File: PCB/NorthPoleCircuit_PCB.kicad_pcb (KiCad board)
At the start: 4 copper layers, 150 x 110 mm, 105 parts, among them J1 USB_C_Receptacle_USB2.0_16P, J2 PROG, J3 PROG, U1 DRV8833PWP, U2 DRV8833PWP, U3 CH32V003FxUx, U4 CH32V003FxUx

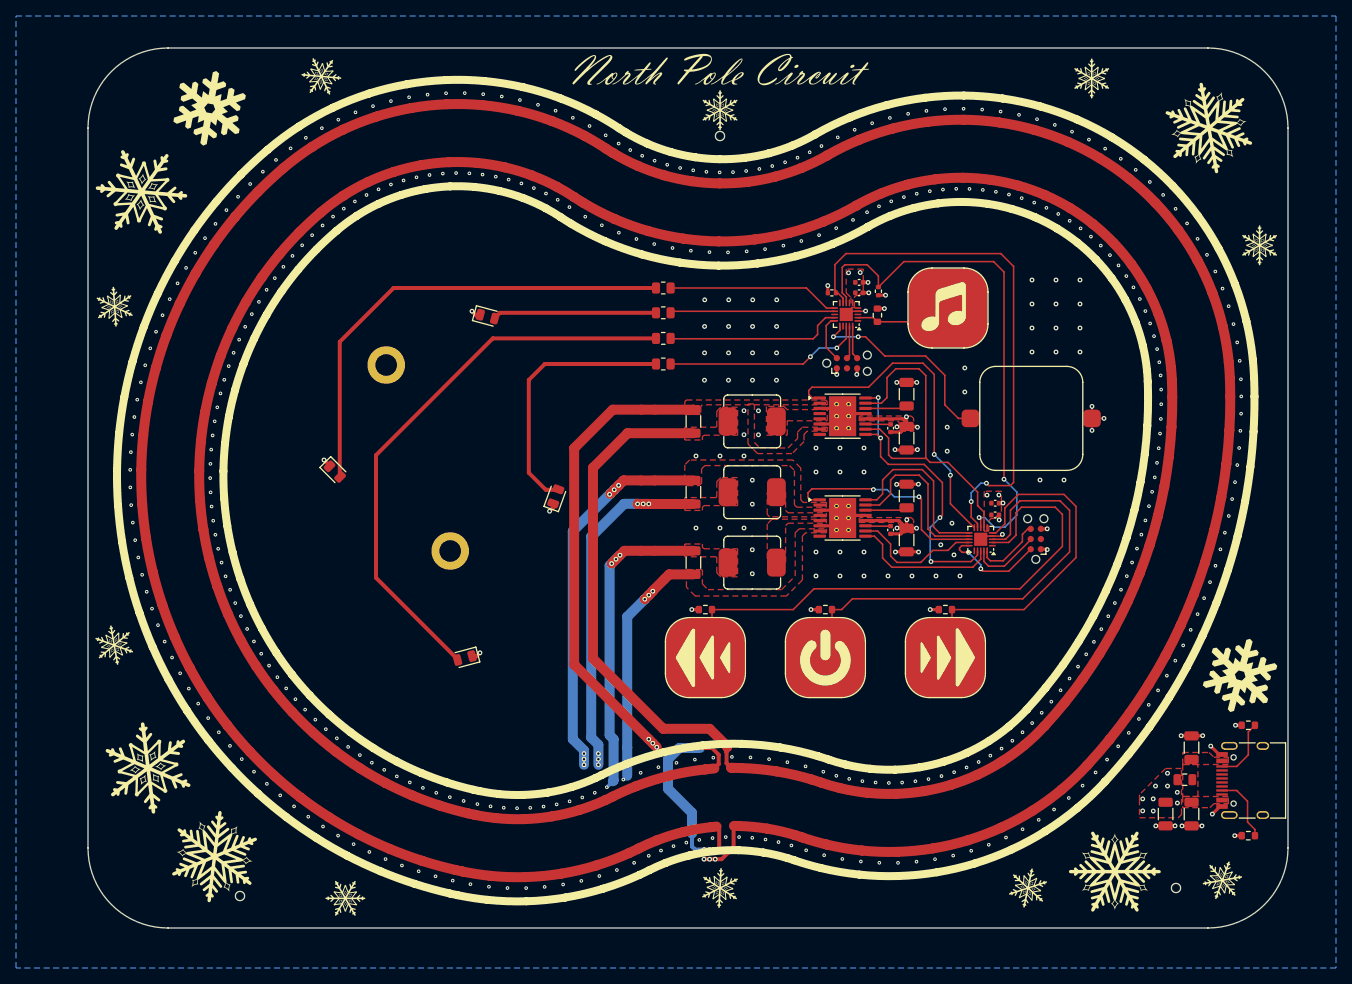
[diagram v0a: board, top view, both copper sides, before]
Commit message: Add BLE audio card hardware revision
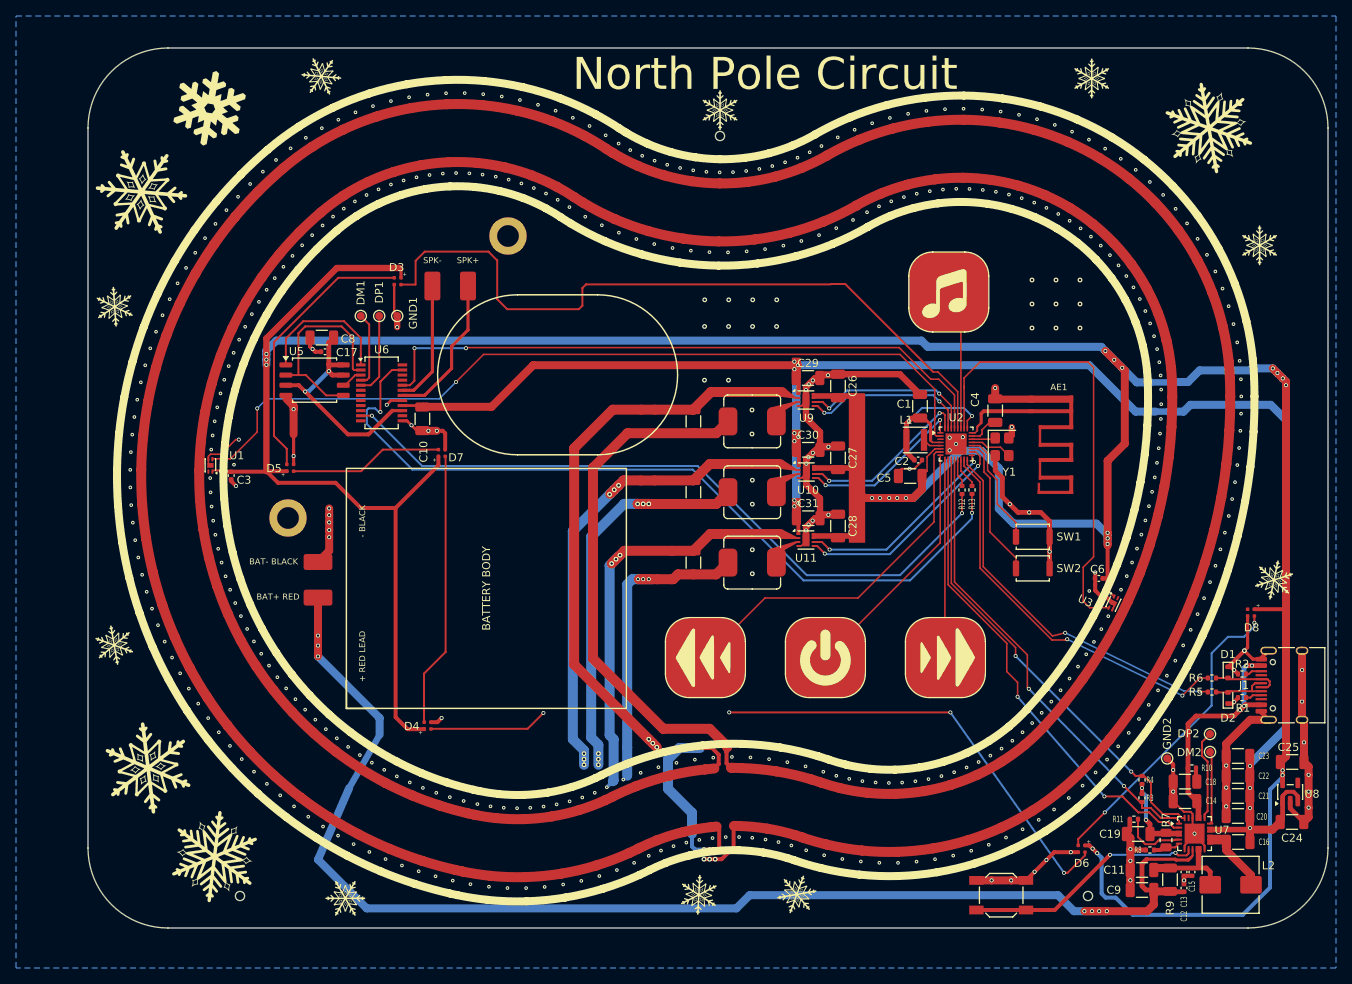
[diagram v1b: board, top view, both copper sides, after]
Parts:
- removed BZ1: FUET-1325H, cust_fp:FUET-1325
- removed the C10 at (165.3, 100.2)
- removed F1: 500mA, Fuse:Fuse_0805_2012Metric
- removed the G*** at (193.3, 142.9)
- removed the G*** at (148.8, 43.4)
- removed the G*** at (208.9, 118.4)
- removed the G*** at (140.8, 121.8)
- removed the G*** at (108.4, 130.2)
- removed the G*** at (108.9, 139.4)
- removed the G*** at (140.0, 67.8)
- removed the G*** at (152.5, 139.7)
- removed the G*** at (133.0, 83.5)
- removed the G*** at (157.6, 130.3)
- removed J2, J3: PROG, Connector:Tag-Connect_TC2030-IDC-NL_2x03_P1.27mm_Vertical
- removed the R3 at (136.9, 76.3)
- removed the R4 at (136.9, 73.1)
- removed U4: CH32V003FxUx, Package_DFN_QFN:QFN-20-1EP_3x3mm_P0.4mm_EP1.65x1.65mm
- added AE1: Bluetooth Antenna, cust_fp:WCH_ANT_F_1_2_4G_1p0mmFR4_12p3x5p6, F.Cu at (183.1, 85.4)
- added BAT_PAD1: BAT_PAD, cust_fp:Battery_LiPo_500mAh_30x35x4mm_WirePads, F.Cu at (93.8, 106.5)
- added BT1_BODY: LiPo_1S_500mAh, cust_fp:Battery_LiPo_500mAh_30x35x4mm_Body, F.Cu at (114.8, 107.5)
- added C11: 10uF, Capacitor_SMD:C_1206_3216Metric, F.Cu at (196.8, 142.8)
- added C12: 100nF, Capacitor_SMD:C_0402_1005Metric, F.Cu at (202.0, 145.0)
- added C16: 2.2uF, Capacitor_SMD:C_1206_3216Metric, F.Cu at (208.8, 139.2)
- added C17: 10uF, Capacitor_SMD:C_1206_3216Metric, F.Cu at (94.2, 76.2)
- added C18: 10uF, Capacitor_SMD:C_1206_3216Metric, F.Cu at (202.1, 131.7)
- added C19: 2.2uF, Capacitor_SMD:C_1206_3216Metric, F.Cu at (196.3, 138.2)
- added C20: 10uF, Capacitor_SMD:C_1206_3216Metric, F.Cu at (208.8, 136.0)
- added C21: 10uF, Capacitor_SMD:C_1206_3216Metric, F.Cu at (208.8, 133.5)
- added C22: 22uF, Capacitor_SMD:C_1206_3216Metric, F.Cu at (208.8, 131.0)
- added C23: 22uF, Capacitor_SMD:C_1206_3216Metric, F.Cu at (208.8, 128.5)
- added C24: 1uF, Capacitor_SMD:C_1206_3216Metric, F.Cu at (215.5, 136.8)
- added C25: 1uF, Capacitor_SMD:C_1206_3216Metric, F.Cu at (215.5, 129.2)
- added C28: 2.2uF, Capacitor_SMD:C_1206_3216Metric, F.Cu at (158.8, 99.8)
- added C31: 10uF, Capacitor_SMD:C_1206_3216Metric, F.Cu at (155.0, 98.8)
- added C4: 470nF, Capacitor_SMD:C_1206_3216Metric, F.Cu at (178.4, 85.3)
- added C5: 2.2uF, Capacitor_SMD:C_1206_3216Metric, F.Cu at (167.8, 93.5)
- added C8: 100nF, Capacitor_SMD:C_0402_1005Metric, F.Cu at (94.6, 78.0)
- added C9: 10uF, Capacitor_SMD:C_1206_3216Metric, F.Cu at (196.8, 145.2)
- added D5: TZ-H1010-RGB/A-BU08UF-TA1305NA/W109, cust_fp:ws2812b_1010, F.Cu at (90.3, 92.5)
- added D6: TZ-H1010-RGB/A-BU08UF-TA1305NA/W109, cust_fp:ws2812b_1010, F.Cu at (189.2, 140.1)
- added D7: TZ-H1010-RGB/A-BU08UF-TA1305NA/W109, cust_fp:ws2812b_1010, F.Cu at (109.2, 90.6)
- added D8: TZ-H1010-RGB/A-BU08UF-TA1305NA/W109, cust_fp:ws2812b_1010, F.Cu at (210.4, 110.6)
- added DM1: TestPoint_Small, TestPoint:TestPoint_Pad_D1.0mm, F.Cu at (99.1, 73.5)
- added DM2: TestPoint_Small, TestPoint:TestPoint_Pad_D1.0mm, F.Cu at (205.2, 128.0)
- added DP1: TestPoint_Small, TestPoint:TestPoint_Pad_D1.0mm, F.Cu at (101.4, 73.5)
- added DP2: TestPoint_Small, TestPoint:TestPoint_Pad_D1.0mm, F.Cu at (205.2, 125.8)
- added GND1: TestPoint_Small, TestPoint:TestPoint_Pad_D1.0mm, F.Cu at (103.7, 73.5)
- added GND2: TestPoint_Small, TestPoint:TestPoint_Pad_D1.0mm, F.Cu at (199.9, 128.8)
- added L1: ZENR3015T100M-10uH, Inductor_SMD:L_Taiyo-Yuden_NR-30xx, F.Cu at (168.4, 89.0)
- added L2: 1uH, Inductor_SMD:L_Wuerth_HCI-7030, F.Cu at (207.8, 144.6)
- added LS1_BODY: GSPK3020035PN-8R0.8W, cust_fp:Speaker_GSPK3020035PN_Body, F.Cu at (123.7, 80.8)
- added R11: 100kΩ, Resistor_SMD:R_0402_1005Metric, F.Cu at (195.7, 136.4)
- added R12: 2.7kΩ, Resistor_SMD:R_0402_1005Metric, F.Cu at (174.2, 95.2)
- added R13: 2.7kΩ, Resistor_SMD:R_0402_1005Metric, F.Cu at (175.5, 95.2)
- added SP_PAD1: SPK_PAD, cust_fp:Speaker_GSPK3020035PN_WirePads, F.Cu at (110.3, 69.8)
- added SW1: TS-1088-AR02016, Button_Switch_SMD:SW_Push_SPST_NO_Alps_SKRK, F.Cu at (183.1, 101.1)
- added SW2: TS-1088-AR02016, Button_Switch_SMD:SW_Push_SPST_NO_Alps_SKRK, F.Cu at (183.1, 105.0)
- added SW3: TS-1187A-C-E-B, Button_Switch_SMD:SW_SPST_SKQG_WithStem, F.Cu at (179.2, 145.9)
- added U10: DRV8837, Package_SON:WSON-8-1EP_2x2mm_P0.5mm_EP0.9x1.6mm, F.Cu at (154.8, 93.0)
- added U11: DRV8837, Package_SON:WSON-8-1EP_2x2mm_P0.5mm_EP0.9x1.6mm, F.Cu at (154.8, 101.5)
- added U5: PY25Q64HA-SUH-IR, Package_SO:SOIC-8_5.3x5.3mm_P1.27mm, F.Cu at (93.3, 81.5)
- added U6: WT2003H4-24SS, Package_SO:SSOP-24_3.9x8.7mm_P0.635mm, F.Cu at (101.7, 83.1)
- added U7: IP5209T, Package_DFN_QFN:QFN-24-1EP_4x4mm_P0.5mm_EP2.5x2.5mm, F.Cu at (203.3, 138.2)
- added U8: ME6211C33M5, Package_TO_SOT_SMD:SOT-23-5, F.Cu at (215.3, 133.0)
- added U9: DRV8837, Package_SON:WSON-8-1EP_2x2mm_P0.5mm_EP0.9x1.6mm, F.Cu at (154.8, 84.0)
- added Y1: 32MHz, Crystal:Crystal_SMD_3225-4Pin_3.2x2.5mm, F.Cu at (179.2, 89.8)
- C1: value 10uF -> 4.7uF
- C10: renamed from C16; value 100n -> 10uF; footprint Capacitor_SMD:C_0402_1005Metric -> Capacitor_SMD:C_1206_3216Metric
- C13, C15: value 100n -> 100nF
- C14: value 100n -> 10uF; footprint Capacitor_SMD:C_0402_1005Metric -> Capacitor_SMD:C_1206_3216Metric
- C2, C3: value 10uF -> 100nF; footprint Capacitor_SMD:C_1206_3216Metric -> Capacitor_SMD:C_0402_1005Metric
- C6: value 10nF -> 100nF
- D1, D2: value LED -> LESD5D5.0CT1G; footprint LED_SMD:LED_0805_2012Metric -> Diode_SMD:D_SOD-523
- D3, D4: value LED -> TZ-H1010-RGB/A-BU08UF-TA1305NA/W109; footprint LED_SMD:LED_0805_2012Metric -> cust_fp:ws2812b_1010
- L3: renamed from L1; value SMMS0650-101M -> 100uH
- L4: renamed from L2; value SMMS0650-101M -> 100uH
- L5: renamed from L3; value SMMS0650-101M -> 100uH
- R1, R2: value 5k1 -> 5.1kΩ; footprint Resistor_SMD:R_0603_1608Metric -> Resistor_SMD:R_0402_1005Metric
- R10: value 510k -> 2Ω; footprint Resistor_SMD:R_0603_1608Metric -> Resistor_SMD:R_0402_1005Metric
- R3: renamed from R11; value 3.3k -> 3.3kΩ
- R4: renamed from R12; value 3.3k -> 3.3kΩ
- R5, R6: value 180R -> 27Ω; footprint Resistor_SMD:R_0805_2012Metric -> Resistor_SMD:R_0402_1005Metric
- R7: value 510k -> 2MΩ; footprint Resistor_SMD:R_0603_1608Metric -> Resistor_SMD:R_0805_2012Metric
- R8: value 510k -> 1MΩ; footprint Resistor_SMD:R_0603_1608Metric -> Resistor_SMD:R_0402_1005Metric
- R9: value 510k -> 10mΩ; footprint Resistor_SMD:R_0603_1608Metric -> Resistor_SMD:R_1206_3216Metric
- U1: value DRV8833PWP -> DRV5032FADMRR; footprint cust_fp:HTSSOP-16-1EP_4.4x5mm_P0.65mm_EP3.4x5mm_Mask2.46x2.31mm_ThermalVias_Larger -> Package_SON:Texas_X2SON-4-1EP_1.1x1.4mm_P0.5mm_EP0.8x0.6mm
- U2: value DRV8833PWP -> CH592X; footprint cust_fp:HTSSOP-16-1EP_4.4x5mm_P0.65mm_EP3.4x5mm_Mask2.46x2.31mm_ThermalVias_Larger -> Package_DFN_QFN:QFN-32-1EP_4x4mm_P0.4mm_EP2.65x2.65mm
- U3: value CH32V003FxUx -> DRV5032FADMRR; footprint Package_DFN_QFN:QFN-20-1EP_3x3mm_P0.4mm_EP1.65x1.65mm -> Package_SON:Texas_X2SON-4-1EP_1.1x1.4mm_P0.5mm_EP0.8x0.6mm
- moved C3 124.2 mm to (82.9, 93.5)
- moved D2 104.1 mm to (207.5, 121.2), turned to 90 degrees
- moved D1 95.4 mm to (207.5, 118.0), turned to -90 degrees
- moved R5 85.2 mm to (205.5, 120.5), turned to 0 degrees
- moved C15 84.6 mm to (203.0, 143.0), turned to -90 degrees
- moved U1 79.3 mm to (80.3, 92.2), turned to 180 degrees
- moved R6 79.0 mm to (205.5, 118.8), turned to 0 degrees
- moved R4 72.2 mm to (196.8, 131.5), turned to 90 degrees
- moved R3 71.4 mm to (196.8, 133.7), turned to -90 degrees
- moved R10 68.9 mm to (203.0, 130.0), turned to 0 degrees
- moved R7 64.4 mm to (199.8, 139.0), turned to -90 degrees
- moved C1 61.2 mm to (169.0, 84.8), turned to 90 degrees
- moved C10 56.8 mm to (106.8, 86.3), turned to -90 degrees
- moved G*** 53.2 mm to (153.6, 145.8)
- moved C13 51.8 mm to (202.0, 143.0), turned to -90 degrees
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- renumbered C5 to C26, C9 to C27, C4 to C29, C8 to C30, C7 to C32, C11 to C33, C12 to C34, H5 to H1, H6 to H2, H9 to H5, H8 to H6, TP3 to TP1, TP4 to TP2, TP5 to TP3, TP6 to TP4
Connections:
- C1 pad 1: VDD -> Net-(U2-VDCIA)
- C13 pad 1: +5V -> Net-(U7-CSIN)
- C14 pad 1: +5V -> Net-(C14-Pad1)
- C15 pad 1: +5V -> Net-(U7-CSIN)
- C2 pad 1: VDD -> Net-(U2-VDCIA)
- C26 pad 2: Net-(U1-VINT) -> +3.3V
- C27 pad 2: Net-(U2-VINT) -> +3.3V
- C3 pad 1: +5V -> +3.3V
- C6 pad 1: +5V -> +3.3V
- C6 pad 2: Net-(U1-VCP) -> GND
- D1 pad 2: Net-(D1-A) -> Net-(D1-A2)
- D2 pad 2: Net-(D2-A) -> Net-(D2-A2)
- D3 pad 1: GND -> Net-(D3-DO)
- D3 pad 2: Net-(D3-A) -> +3.3V
- D4 pad 1: GND -> Net-(D4-DO)
- D4 pad 2: Net-(D4-A) -> +3.3V
- J1 pad A4: VDD -> Net-(C14-Pad1)
- J1 pad A6: unconnected-(J1-D+-PadA6) -> Net-(D1-A2)
- J1 pad A7: unconnected-(J1-D--PadA7) -> Net-(D2-A2)
- J1 pad A9: VDD -> Net-(C14-Pad1)
- J1 pad B4: VDD -> Net-(C14-Pad1)
- J1 pad B6: unconnected-(J1-D+-PadB6) -> Net-(D1-A2)
- J1 pad B7: unconnected-(J1-D--PadB7) -> Net-(D2-A2)
- J1 pad B9: VDD -> Net-(C14-Pad1)
- L3 pad 1: Net-(U1-AOUT2) -> Net-(U9-OUT2)
- L4 pad 1: Net-(U2-AOUT2) -> Net-(U10-OUT2)
- L5 pad 1: Net-(U2-BOUT2) -> Net-(U11-OUT2)
- R10 pad 1: +5V -> Net-(C14-Pad1)
- R10 pad 2: /MUSIC -> Net-(C18-Pad1)
- R3 pad 1: +5V -> /VREG
- R4 pad 1: +5V -> /VREG
- R5 pad 1: /LED1 -> /DN
- R5 pad 2: Net-(D3-A) -> Net-(D2-A2)
- R6 pad 1: /LED4 -> /DP
- R6 pad 2: Net-(D4-A) -> Net-(D1-A2)
- R7 pad 1: +5V -> /VREG
- R7 pad 2: /SPD-- -> Net-(U7-NTC)
- R8 pad 1: +5V -> Net-(U7-NTC)
- R8 pad 2: /RUN -> GND
- R9 pad 1: +5V -> Net-(U7-CSIN)
- R9 pad 2: /SPD++ -> Net-(U7-VBAT)
- U1 pad 1: /SLEEP_G -> +3.3V
- U1 pad 2: /G1_OUT -> /HALL1
- U1 pad 4: Net-(U1-AOUT2) -> unconnected-(U1-NC-Pad4)
- U1 pad 5: Net-(U1-AOUT2) -> GND
- U2 pad 1: /SLEEP_PH -> /PWM_A2
- U2 pad 10: /PWM_B2 -> /INT
- U2 pad 11: Net-(U2-VCP) -> /SCL
- U2 pad 12: +5V -> /SDA
- U2 pad 13: GND -> Net-(U2-PB13)
- U2 pad 14: Net-(U2-VINT) -> Net-(U2-PB12)
- U2 pad 15: /PWM_A2 -> /DP
- U2 pad 16: /PWM_A1 -> /DN
- U2 pad 17: GND -> /PWM_B1
- U2 pad 2: /A1_OUT -> /HALL1
- U2 pad 3: GND -> unconnected-(U2-PB0-Pad3)
- U2 pad 4: Net-(U2-AOUT2) -> Net-(U2-VDCIA)
- U2 pad 5: Net-(U2-BOUT2) -> Net-(U2-VSW)
- U2 pad 6: GND -> +3.3V
- U2 pad 7: /B1_OUT -> /SPD--
- U2 pad 8: unconnected-(U2-~{FAULT}-Pad8) -> /RUN
- U2 pad 9: /PWM_B1 -> /SPD++
- U3 pad 1: unconnected-(U3-PD7-Pad1) -> +3.3V
- U3 pad 2: /SPD-- -> /HALL2
- U3 pad 3: /RUN -> GND
- U3 pad 4: GND -> unconnected-(U3-NC-Pad4)
- U3 pad 5: /SPD++ -> GND
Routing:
- net +3.3V: track 0.00 -> 434.2 mm, vias 0 -> 22
- net Net-(U7-VBAT): track 0.00 -> 169.3 mm, vias 0 -> 7
- net +5V: track 30.5 -> 190.4 mm, vias 27 -> 13
- net GND: track 61.8 -> 218.2 mm, vias 100 -> 88
- net /HALL1: track 0.00 -> 105.7 mm, vias 0 -> 2
- net /TX1: track 4.24 -> 100.4 mm, vias 0 -> 2
- net Net-(D4-DO): track 0.00 -> 94.4 mm, vias 0 -> 4
- net /LED: track 0.00 -> 91.6 mm
- net /RX1: track 4.13 -> 89.0 mm, vias 0 -> 2
- net /BUSY: track 0.00 -> 80.4 mm, vias 0 -> 2
- net Net-(D1-A): track 70.9 -> 0.00 mm
- net /INT: track 0.00 -> 60.7 mm, vias 0 -> 2
- net Net-(D3-A): track 59.2 -> 0.00 mm
- net /HALL2: track 0.00 -> 57.1 mm
- net /DP: track 0.00 -> 49.1 mm, vias 0 -> 2
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- removed copper zone on F.Cu, net +5V
- removed copper zone on F.Cu, net /A1_OUT
- removed copper zone on F.Cu, net /A2_OUT
- removed copper zone on F.Cu, net /B1_OUT
- removed copper zone on F.Cu, net /B2_OUT
- removed copper zone on F.Cu, net /G1_OUT
- removed copper zone on F.Cu, net /G2_OUT
- removed copper zone on F.Cu, net Net-(U1-AOUT2)
- removed copper zone on F.Cu, net Net-(U2-AOUT2)
- removed copper zone on F.Cu, net Net-(U2-BOUT2)
- removed copper zone on F.Cu, net VDD
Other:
- board size 150 x 110 mm -> 155 x 110 mm
- board text added: "And a Happy New Year"
- board text added: "Inspired by Janky Jingle Crew 2024 Card"
- board text added: "Merry Christmas"
- board text added: "North Pole Circuit"
- board text added: "Sergey Lukin"

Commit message: Schematics and PCB update. Fiirmware v0.1
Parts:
- removed DM1, DP1, GND1: TestPoint_Small, TestPoint:TestPoint_Pad_D1.0mm
- added G***: LOGO, cust_fp:LOGO, F.Cu at (124.2, 98.3)
- added J3: PROG, Connector:Tag-Connect_TC2030-IDC-NL_2x03_P1.27mm_Vertical, F.Cu at (173.5, 103.5)
- added J4: PROG, Connector:Tag-Connect_TC2030-IDC-NL_2x03_P1.27mm_Vertical, F.Cu at (99.3, 72.4)
- added R14: 0Ω, Resistor_SMD:R_0402_1005Metric, F.Cu at (173.2, 109.1)
- added R15: 0Ω, Resistor_SMD:R_0402_1005Metric, F.Cu at (173.2, 108.0)
- added R16: 100kΩ, Resistor_SMD:R_0402_1005Metric, F.Cu at (166.2, 83.6)
- G***: footprint LOGO -> cust_fp:LOGO
- moved C17 18.9 mm to (109.2, 87.7), turned to -90 degrees
- moved SP_PAD1 6.33 mm to (106.5, 74.8), turned to 90 degrees
- moved LS1_BODY 1.66 mm to (123.9, 79.2)
- moved G*** 0.71 mm to (140.8, 105.4)
- moved C1 0.55 mm to (168.4, 84.8)
- moved D7 0.48 mm to (109.2, 91.1)
- moved L1 0.45 mm to (167.9, 89.0)
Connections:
- U10 pad 7: +3.3V -> /SLEEP
- U11 pad 7: +3.3V -> /SLEEP
- U2 pad 11: /SCL -> /SWDCK
- U2 pad 12: /SDA -> /SWDIO
- U2 pad 3: unconnected-(U2-PB0-Pad3) -> /SLEEP
- U9 pad 7: +3.3V -> /SLEEP
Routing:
- net /SLEEP: track 0.00 -> 46.3 mm, vias 0 -> 4
- net +5V: track 190.4 -> 216.4 mm
- net /SWDCK: track 0.00 -> 22.7 mm
- net /SWDIO: track 0.00 -> 20.5 mm, vias 0 -> 2
- net /SCL: track 58.8 -> 41.6 mm
- net /SDA: track 58.9 -> 42.7 mm
- net +3.3V: track 434.2 -> 442.5 mm, vias 22 -> 23
- net Net-(U6-PWM-): track 15.4 -> 7.48 mm
- net /INT: track 60.7 -> 66.4 mm
- net /VOUT: track 30.6 -> 35.6 mm
- net /SPD++: track 24.7 -> 29.6 mm
- net /DO: track 26.2 -> 22.9 mm
- net Net-(U5-~{CS}): track 17.8 -> 14.9 mm
- net Net-(U6-PWM+): track 18.7 -> 15.9 mm
- net GND: track 218.2 -> 220.9 mm, vias 88 -> 89
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
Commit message: Final PCB update before ordering. Firmware update based on the CH592 Dev Board.
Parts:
- added +3.3V1: +3.3V, TestPoint:TestPoint_Pad_D1.5mm, F.Cu at (217.1, 107.8)
- added +5V1: +5V, TestPoint:TestPoint_Pad_D1.5mm, F.Cu at (215.6, 142.2)
- added A1: A1, TestPoint:TestPoint_Pad_D1.5mm, F.Cu at (158.8, 95.2)
- added A2: A2, TestPoint:TestPoint_Pad_D1.5mm, F.Cu at (156.5, 96.3)
- added B1: B1, TestPoint:TestPoint_Pad_D1.5mm, F.Cu at (159.4, 103.8)
- added B2: B2, TestPoint:TestPoint_Pad_D1.5mm, F.Cu at (156.8, 105.7)
- added FID1: Fiducial, Fiducial:Fiducial_0.75mm_Mask1.5mm, F.Cu at (68.5, 50.0)
- added FID2: Fiducial, Fiducial:Fiducial_0.75mm_Mask1.5mm, F.Cu at (215.0, 50.0)
- added FID3: Fiducial, Fiducial:Fiducial_0.75mm_Mask1.5mm, F.Cu at (68.5, 138.0)
- added G***: Bluetooth_Logo_6.0x6.0mm_SilkScreen, NorthPole_Logos:Bluetooth_Logo_6.0x6.0mm_SilkScreen, F.Cu at (182.4, 73.7)
- added G1: G1, TestPoint:TestPoint_Pad_D1.5mm, F.Cu at (158.8, 86.1)
- added G2: G2, TestPoint:TestPoint_Pad_D1.5mm, F.Cu at (156.9, 87.8)
- added GND3: HALL2, TestPoint:TestPoint_Pad_D1.5mm, F.Cu at (154.1, 105.8)
- added HALL1: HALL1, TestPoint:TestPoint_Pad_D1.5mm, F.Cu at (84.8, 87.1)
- added HALL2: HALL2, TestPoint:TestPoint_Pad_D1.5mm, F.Cu at (186.6, 109.7)
- added LED1: LED, TestPoint:TestPoint_Pad_D1.5mm, F.Cu at (161.7, 68.2)
- added REF**: OSHW-Logo_5.7x6mm_SilkScreen, Symbol:OSHW-Logo_5.7x6mm_SilkScreen, F.Cu at (142.9, 73.3)
- added REF**: WEEE-Logo_5.6x8mm_SilkScreen, Symbol:WEEE-Logo_5.6x8mm_SilkScreen, F.Cu at (188.2, 74.7)
- added REF**: KiCad-Logo2_5mm_SilkScreen, Symbol:KiCad-Logo2_5mm_SilkScreen, B.Cu at (72.4, 120.8)
- added SCL1: SCL, TestPoint:TestPoint_Pad_D1.5mm, F.Cu at (180.7, 118.4)
- added SDA1: SDA, TestPoint:TestPoint_Pad_D1.5mm, F.Cu at (184.6, 116.7)
- added SLEEP1: SLEEP, TestPoint:TestPoint_Pad_D1.5mm, F.Cu at (164.2, 86.3)
- moved G*** 1.95 mm to (211.3, 106.6)
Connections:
- J4 pad 1: +5V -> unconnected-(J4-VCC-Pad1)
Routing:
- net +5V: track 216.4 -> 196.0 mm
- net GND: track 220.9 -> 225.5 mm
- net /PWM_B2: track 28.1 -> 30.7 mm
- net /SCL: track 41.6 -> 44.1 mm
- net +3.3V: track 442.5 -> 444.9 mm
- net /PWM_G2: track 21.1 -> 23.3 mm
- net /PWM_B1: track 25.9 -> 28.1 mm
- net /SDA: track 42.7 -> 44.8 mm
- net /PWM_A2: track 21.1 -> 23.1 mm
- net /PWM_G1: track 22.1 -> 23.7 mm
- net /PWM_A1: track 22.0 -> 23.5 mm
- net /HALL1: track 105.7 -> 107.0 mm
- net /LED: track 91.6 -> 90.5 mm
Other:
- board text added: "DM"
- board text added: "DP"
- board text added: "G"
